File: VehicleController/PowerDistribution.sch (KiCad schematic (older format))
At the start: 15 parts, among them P3 RPi_USB_PWR, U2 TL431, U3 BTS6133D, U4 AP1117

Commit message: Nearly finished with VC Schematic
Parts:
- P3: symbol USB_A -> USB_A-RESCUE-VehicleController
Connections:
- net 5V renamed +5V
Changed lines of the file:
@@
 EESchema Schematic File Version 2
+LIBS:UNCAMotorsports
 LIBS:VehicleController-rescue
 LIBS:power
@@
 LIBS:contrib
 LIBS:valves
-LIBS:UNCAMotorsports
 LIBS:Common-Parts-Library-CPL
 LIBS:relays
@@
 $EndComp
 $Comp
-L GND #PWR26
+L GND #PWR026
 U 1 1 587C7BE3
 P 6000 3550
-F 0 "#PWR26" H 6000 3300 50  0001 C CNN
+F 0 "#PWR026" H 6000 3300 50  0001 C CNN
 F 1 "GND" H 6005 3377 50  0000 C CNN
 F 2 "" H 6000 3550 50  0000 C CNN
@@
 $EndComp
 $Comp
-L GND #PWR24
+L GND #PWR027
 U 1 1 587C7BF7
 P 4300 4700
-F 0 "#PWR24" H 4300 4450 50  0001 C CNN
+F 0 "#PWR027" H 4300 4450 50  0001 C CNN
 F 1 "GND" H 4305 4527 50  0000 C CNN
 F 2 "" H 4300 4700 50  0000 C CNN
@@
 $EndComp
 $Comp
-L GND #PWR28
+L GND #PWR028
 U 1 1 58AEB860
 P 8100 3250
-F 0 "#PWR28" H 8100 3000 50  0001 C CNN
+F 0 "#PWR028" H 8100 3000 50  0001 C CNN
 F 1 "GND" H 8105 3077 50  0000 C CNN
 F 2 "" H 8100 3250 50  0000 C CNN
@@
 Text HLabel 7350 2550 1    60   Input ~ 0
 12V
-Text HLabel 8900 2750 2    60   Input ~ 0
+Text HLabel 8850 2750 2    60   Input ~ 0
 5V
 $Comp
-L PWR_FLAG #FLG2
+L PWR_FLAG #FLG029
 U 1 1 58AF2028
 P 5550 1000
-F 0 "#FLG2" H 5550 1095 50  0001 C CNN
+F 0 "#FLG029" H 5550 1095 50  0001 C CNN
 F 1 "PWR_FLAG" H 5550 1224 50  0001 C CNN
 F 2 "" H 5550 1000 50  0000 C CNN
@@
 12V
 $Comp
-L PWR_FLAG #FLG3
-U 1 1 58AF2853
-P 5700 1000
-F 0 "#FLG3" H 5700 1095 50  0001 C CNN
-F 1 "PWR_FLAG" H 5700 1224 50  0001 C CNN
-F 2 "" H 5700 1000 50  0000 C CNN
-F 3 "" H 5700 1000 50  0000 C CNN
-	1    5700 1000
-	1    0    0    -1
-$EndComp
-$Comp
-L GND #PWR25
-U 1 1 58AF29E4
-P 5700 1200
-F 0 "#PWR25" H 5700 950 50  0001 C CNN
-F 1 "GND" H 5705 1027 50  0000 C CNN
-F 2 "" H 5700 1200 50  0000 C CNN
-F 3 "" H 5700 1200 50  0000 C CNN
-	1    5700 1200
-	1    0    0    -1
-$EndComp
-Text HLabel 5400 1200 3    60   Input ~ 0
-PWR_IN
-$Comp
-L PWR_FLAG #FLG1
-U 1 1 58AF2E1D
-P 5400 1000
-F 0 "#FLG1" H 5400 1095 50  0001 C CNN
-F 1 "PWR_FLAG" H 5400 1224 50  0000 C CNN
-F 2 "" H 5400 1000 50  0000 C CNN
-F 3 "" H 5400 1000 50  0000 C CNN
-	1    5400 1000
-	1    0    0    -1
-$EndComp
-$Comp
-L USB_A P3
+L USB_A-RESCUE-VehicleController P3
 U 1 1 58B30D8B
 P 8050 4350
+AR Path="/58B30D8B" Ref="P3"  Part="1"
+AR Path="/587C78BB/58B30D8B" Ref="P3"  Part="1"
 F 0 "P3" V 7625 4274 50  0000 C CNN
 F 1 "RPi_USB_PWR" V 7716 4274 50  0000 C CNN
@@
 $EndComp
 $Comp
-L GND #PWR27
+L GND #PWR030
 U 1 1 58B30D9F
 P 7950 4750
-F 0 "#PWR27" H 7950 4500 50  0001 C CNN
+F 0 "#PWR030" H 7950 4500 50  0001 C CNN
 F 1 "GND" H 7955 4577 50  0000 C CNN
 F 2 "" H 7950 4750 50  0000 C CNN
@@
 12V
 $Comp
-L GND #PWR29
+L GND #PWR031
 U 1 1 58B31164
 P 8700 4550
-F 0 "#PWR29" H 8700 4300 50  0001 C CNN
+F 0 "#PWR031" H 8700 4300 50  0001 C CNN
 F 1 "GND" H 8705 4377 50  0000 C CNN
 F 2 "" H 8700 4550 50  0000 C CNN
@@
 $EndComp
 $Comp
-L GND #PWR22
+L GND #PWR032
 U 1 1 58B0EFE3
 P 3350 3250
-F 0 "#PWR22" H 3350 3000 50  0001 C CNN
+F 0 "#PWR032" H 3350 3000 50  0001 C CNN
 F 1 "GND" H 3355 3077 50  0000 C CNN
 F 2 "" H 3350 3250 50  0000 C CNN
@@
 $EndComp
 $Comp
-L GND #PWR23
+L GND #PWR033
 U 1 1 58B0F09D
 P 3550 3250
-F 0 "#PWR23" H 3550 3000 50  0001 C CNN
+F 0 "#PWR033" H 3550 3000 50  0001 C CNN
 F 1 "GND" H 3555 3077 50  0000 C CNN
 F 2 "" H 3550 3250 50  0000 C CNN
@@
 	4300 4250 4300 4700
 Wire Wire Line
-	4300 4400 4850 4400
-Wire Wire Line
-	4850 4400 4850 4150
+	4850 4400 4300 4400
+Wire Wire Line
+	4850 4150 4850 4400
 Connection ~ 4300 4400
 Wire Wire Line
@@
 	8600 2900 8600 2750
 Wire Wire Line
-	8400 2750 8900 2750
+	8400 2750 8850 2750
 Connection ~ 7600 2750
 Connection ~ 8600 2750
@@
 Wire Wire Line
 	5550 1200 5550 1000
-Wire Wire Line
-	5700 1200 5700 1000
-Wire Wire Line
-	5400 1200 5400 1000
 Connection ~ 8550 4150
 Wire Wire Line
@@
 Wire Wire Line
 	4850 2850 4850 3550
+$Comp
+L +5V #PWR034
+U 1 1 58BE7A1A
+P 8750 2600
+F 0 "#PWR034" H 8800 2650 50  0001 C CNN
+F 1 "+5V" H 8765 2773 50  0000 C CNN
+F 2 "" H 0   -100 50  0001 C CNN
+F 3 "" H 0   -100 50  0001 C CNN
+	1    8750 2600
+	1    0    0    -1
+$EndComp
+Wire Wire Line
+	8750 2600 8750 2750
+Connection ~ 8750 2750
 $EndSCHEMATC

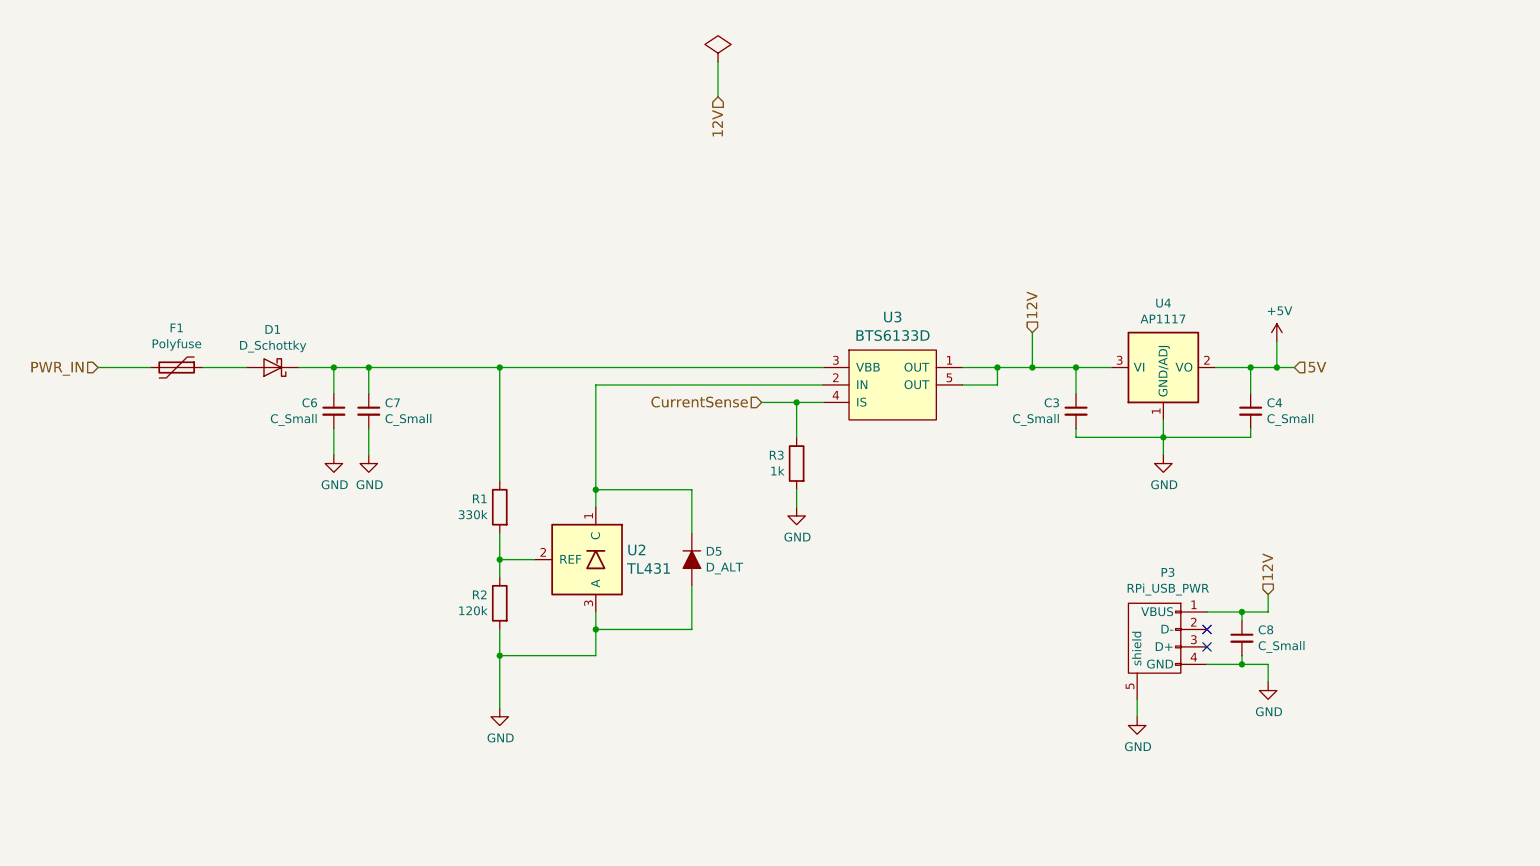
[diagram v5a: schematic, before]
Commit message: More status LEDs and fuses
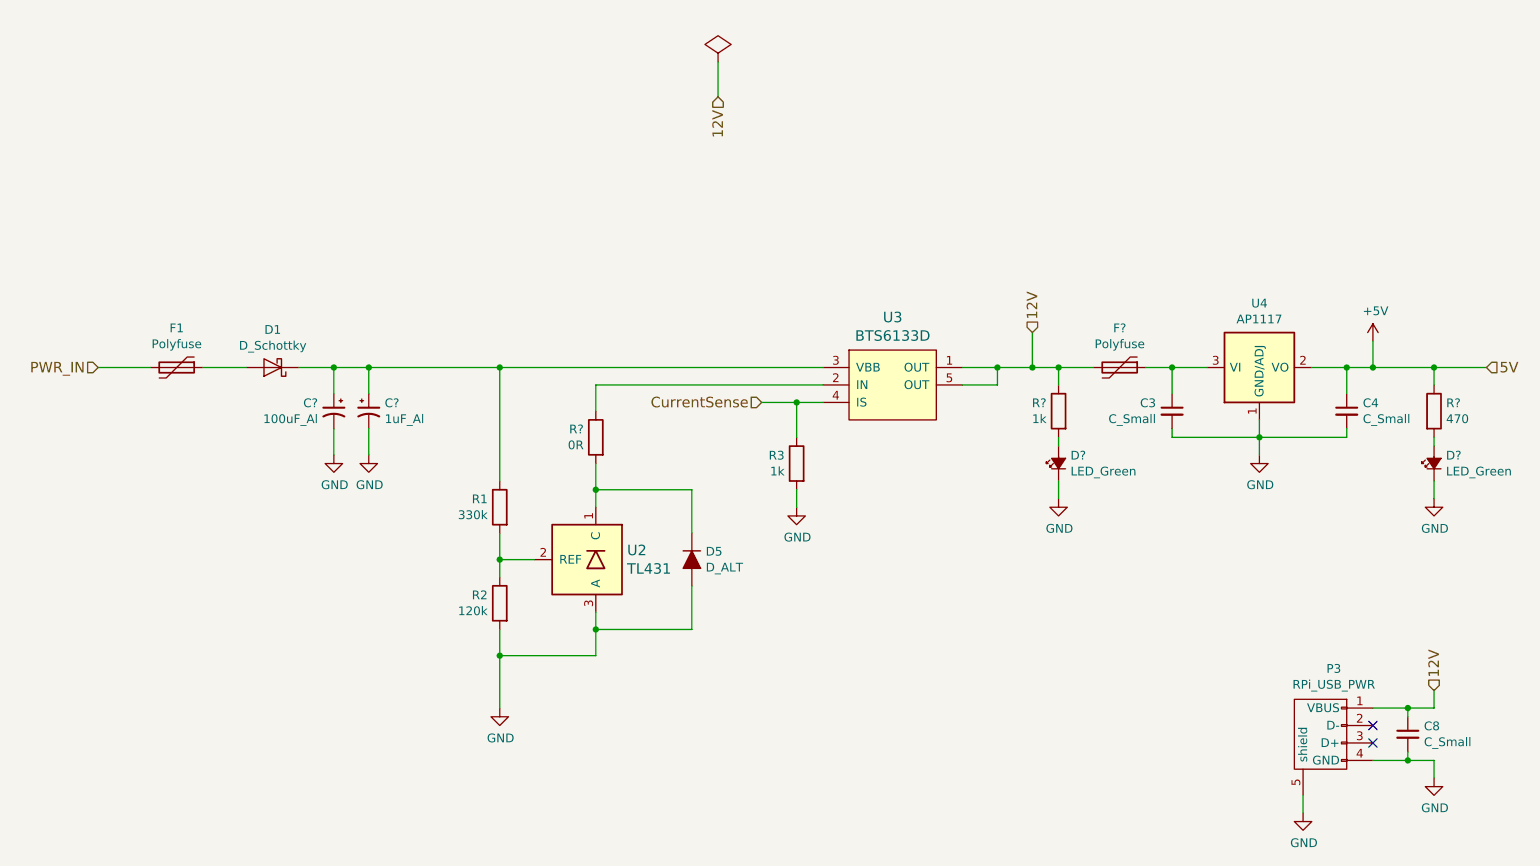
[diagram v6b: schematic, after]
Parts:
- removed C6, C7: C_Small, symbol C_Small
- added C?: 100uF_Al, symbol CP1_Small
- added C?: 1uF_Al, symbol CP1_Small
- added D? (x2): LED_Green, symbol LED_Small_ALT
- added F?: Polyfuse, symbol Polyfuse
- added R?: 1k, symbol R
- added R?: 470, symbol R
- added R?: 0R, symbol R
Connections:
- net +5V: now also R?.1
- net 12V: now also F?.2, R?.1; no longer C3.1, U4.3 (VI)
- net GND: now also C?.2, C?.2, D?.1 (K), D?.1 (K)
- net at D1.1 (K), R1.1, U3.3 (VBB): now also C?.1, C?.1
- net at D5.1 (K), U2.1 (C): now also R?.2; no longer U3.2 (IN)
- new net: R?.1, U3.2 (IN)
- new net: C3.1, F?.1, U4.3 (VI)
- new net: D?.2 (A), R?.2 (x2)
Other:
- moved on the sheet: C3, C4, C8, P3

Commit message: Begin nailing down VC schematic details
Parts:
- removed C8: C_Small, symbol C_Small
- removed U4: AP1117, TO_SOT_Packages_SMD:SOT-223, symbol AP1117
- added C9: 1uF_Al, symbol CP1_Small
- added U8: R-78E5.0-1.0, symbol R-78E5.0-1.0
- D6: renamed from D?; value LED_Green -> 12V_Status
- D7: renamed from D?; value LED_Green -> 5V_Status
- R14: renamed from R?; value 1k -> 2.2k
- gave numbers to parts that had none: 5
- renumbered C3 to C7, C4 to C8, D1 to D4, F1 to F2, P3 to P2, R1 to R10, R2 to R11, R3 to R13, U2 to U6, U3 to U7
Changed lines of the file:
@@
 $EndDescr
 $Comp
-L D_Schottky D1
+L D_Schottky D4
 U 1 1 587C7BB2
 P 3000 2750
-F 0 "D1" H 3000 2534 50  0000 C CNN
+F 0 "D4" H 3000 2534 50  0000 C CNN
 F 1 "D_Schottky" H 3000 2625 50  0000 C CNN
 F 2 "" H 3000 2750 50  0000 C CNN
@@
 $EndComp
 $Comp
-L Polyfuse F1
+L Polyfuse F2
 U 1 1 587C7BB9
 P 2450 2750
-F 0 "F1" V 2225 2750 50  0000 C CNN
+F 0 "F2" V 2225 2750 50  0000 C CNN
 F 1 "Polyfuse" V 2316 2750 50  0000 C CNN
 F 2 "" H 2500 2550 50  0001 L CNN
@@
 $EndComp
 $Comp
-L TL431 U2
+L TL431 U6
 U 1 1 587C7BC0
 P 4850 3850
-F 0 "U2" H 4671 3903 60  0000 R CNN
+F 0 "U6" H 4671 3903 60  0000 R CNN
 F 1 "TL431" H 4671 3797 60  0000 R CNN
 F 2 "" H 4850 3800 60  0000 C CNN
@@
 $EndComp
 $Comp
-L BTS6133D U3
+L BTS6133D U7
 U 1 1 587C7BC7
 P 6550 2850
-F 0 "U3" H 6550 3237 60  0000 C CNN
+F 0 "U7" H 6550 3237 60  0000 C CNN
 F 1 "BTS6133D" H 6550 3131 60  0000 C CNN
 F 2 "" H 6700 3050 60  0000 C CNN
@@
 $EndComp
 $Comp
-L R R1
+L R R10
 U 1 1 587C7BCE
 P 4300 3550
-F 0 "R1" H 4369 3596 50  0000 L CNN
+F 0 "R10" H 4369 3596 50  0000 L CNN
 F 1 "330k" H 4369 3505 50  0000 L CNN
 F 2 "" V 4230 3550 50  0000 C CNN
@@
 $EndComp
 $Comp
-L R R2
+L R R11
 U 1 1 587C7BD5
 P 4300 4100
-F 0 "R2" H 4369 4146 50  0000 L CNN
+F 0 "R11" H 4369 4146 50  0000 L CNN
 F 1 "120k" H 4369 4055 50  0000 L CNN
 F 2 "" V 4230 4100 50  0000 C CNN
@@
 $EndComp
 $Comp
-L R R3
+L R R13
 U 1 1 587C7BDC
 P 6000 3300
-F 0 "R3" H 6069 3346 50  0000 L CNN
+F 0 "R13" H 6069 3346 50  0000 L CNN
 F 1 "1k" H 6069 3255 50  0000 L CNN
 F 2 "" V 5930 3300 50  0000 C CNN
@@
 $EndComp
 $Comp
-L GND #PWR026
+L GND #PWR29
 U 1 1 587C7BE3
 P 6000 3550
-F 0 "#PWR026" H 6000 3300 50  0001 C CNN
+F 0 "#PWR29" H 6000 3300 50  0001 C CNN
 F 1 "GND" H 6005 3377 50  0000 C CNN
 F 2 "" H 6000 3550 50  0000 C CNN
@@
 $EndComp
 $Comp
-L GND #PWR027
+L GND #PWR28
 U 1 1 587C7BF7
 P 4300 4700
-F 0 "#PWR027" H 4300 4450 50  0001 C CNN
+F 0 "#PWR28" H 4300 4450 50  0001 C CNN
 F 1 "GND" H 4305 4527 50  0000 C CNN
 F 2 "" H 4300 4700 50  0000 C CNN
@@
 CurrentSense
 $Comp
-L C_Small C3
+L C_Small C7
 U 1 1 58AEB852
 P 8150 3000
-F 0 "C3" H 8242 3046 50  0000 L CNN
+F 0 "C7" H 8242 3046 50  0000 L CNN
 F 1 "C_Small" H 8242 2955 50  0000 L CNN
 F 2 "" H 8150 3000 50  0000 C CNN
@@
 $EndComp
 $Comp
-L C_Small C4
+L C_Small C8
 U 1 1 58AEB859
 P 9150 3000
-F 0 "C4" H 9242 3046 50  0000 L CNN
+F 0 "C8" H 9242 3046 50  0000 L CNN
 F 1 "C_Small" H 9242 2955 50  0000 L CNN
 F 2 "" H 9150 3000 50  0000 C CNN
@@
 $EndComp
 $Comp
-L GND #PWR028
+L GND #PWR31
 U 1 1 58AEB860
 P 8650 3250
-F 0 "#PWR028" H 8650 3000 50  0001 C CNN
+F 0 "#PWR31" H 8650 3000 50  0001 C CNN
 F 1 "GND" H 8655 3077 50  0000 C CNN
 F 2 "" H 8650 3250 50  0000 C CNN
@@
 5V
 $Comp
-L PWR_FLAG #FLG029
+L PWR_FLAG #FLG3
 U 1 1 58AF2028
 P 5550 1000
-F 0 "#FLG029" H 5550 1095 50  0001 C CNN
+F 0 "#FLG3" H 5550 1095 50  0001 C CNN
 F 1 "PWR_FLAG" H 5550 1224 50  0001 C CNN
 F 2 "" H 5550 1000 50  0000 C CNN
@@
 12V
 $Comp
-L USB_A-RESCUE-VehicleController P3
+L USB_A-RESCUE-VehicleController P2
 U 1 1 58B30D8B
 P 9000 4900
-AR Path="/58B30D8B" Ref="P3"  Part="1"
-AR Path="/587C78BB/58B30D8B" Ref="P3"  Part="1"
-F 0 "P3" V 8575 4824 50  0000 C CNN
+F 0 "P2" V 8575 4824 50  0000 C CNN
 F 1 "RPi_USB_PWR" V 8666 4824 50  0000 C CNN
 F 2 "" V 8950 4800 50  0000 C CNN
@@
 $EndComp
 $Comp
-L C_Small C8
-U 1 1 58B30D92
-P 9500 4850
-F 0 "C8" H 9592 4896 50  0000 L CNN
-F 1 "C_Small" H 9592 4805 50  0000 L CNN
-F 2 "" H 9500 4850 50  0000 C CNN
-F 3 "" H 9500 4850 50  0000 C CNN
-	1    9500 4850
-	1    0    0    -1
-$EndComp
-$Comp
-L GND #PWR030
+L GND #PWR32
 U 1 1 58B30D9F
 P 8900 5300
-F 0 "#PWR030" H 8900 5050 50  0001 C CNN
+F 0 "#PWR32" H 8900 5050 50  0001 C CNN
 F 1 "GND" H 8905 5127 50  0000 C CNN
 F 2 "" H 8900 5300 50  0000 C CNN
@@
 12V
 $Comp
-L GND #PWR031
+L GND #PWR35
 U 1 1 58B31164
 P 9650 5100
-F 0 "#PWR031" H 9650 4850 50  0001 C CNN
+F 0 "#PWR35" H 9650 4850 50  0001 C CNN
 F 1 "GND" H 9655 4927 50  0000 C CNN
 F 2 "" H 9650 5100 50  0000 C CNN
@@
 $EndComp
 $Comp
-L GND #PWR032
+L GND #PWR26
 U 1 1 58B0EFE3
 P 3350 3250
-F 0 "#PWR032" H 3350 3000 50  0001 C CNN
+F 0 "#PWR26" H 3350 3000 50  0001 C CNN
 F 1 "GND" H 3355 3077 50  0000 C CNN
 F 2 "" H 3350 3250 50  0000 C CNN
@@
 $EndComp
 $Comp
-L GND #PWR033
+L GND #PWR27
 U 1 1 58B0F09D
 P 3550 3250
-F 0 "#PWR033" H 3550 3000 50  0001 C CNN
+F 0 "#PWR27" H 3550 3000 50  0001 C CNN
 F 1 "GND" H 3555 3077 50  0000 C CNN
 F 2 "" H 3550 3250 50  0000 C CNN
@@
 	4850 3300 4850 3550
 $Comp
-L +5V #PWR034
+L +5V #PWR33
 U 1 1 58BE7A1A
 P 9300 2600
-F 0 "#PWR034" H 9350 2650 50  0001 C CNN
+F 0 "#PWR33" H 9350 2650 50  0001 C CNN
 F 1 "+5V" H 9315 2773 50  0000 C CNN
 F 2 "" H 550 -100 50  0001 C CNN
@@
 Connection ~ 9300 2750
 $Comp
-L AP1117 U4
-U 1 1 58C28B86
-P 8650 2750
-F 0 "U4" H 8650 3117 50  0000 C CNN
-F 1 "AP1117" H 8650 3026 50  0000 C CNN
-F 2 "TO_SOT_Packages_SMD:SOT-223" H 500 -350 50  0001 C CNN
-F 3 "" H 600 -250 50  0001 C CNN
-	1    8650 2750
-	1    0    0    -1
-$EndComp
-$Comp
-L Polyfuse F?
+L Polyfuse F3
 U 1 1 58C2ADFE
 P 7850 2750
-F 0 "F?" V 7625 2750 50  0000 C CNN
+F 0 "F3" V 7625 2750 50  0000 C CNN
 F 1 "Polyfuse" V 7716 2750 50  0000 C CNN
 F 2 "" H 7900 2550 50  0001 L CNN
@@
 $EndComp
 $Comp
-L R R?
+L R R14
 U 1 1 58C314B1
 P 7500 3000
-F 0 "R?" H 7569 3046 50  0000 L CNN
-F 1 "1k" H 7569 2955 50  0000 L CNN
+F 0 "R14" H 7569 3046 50  0000 L CNN
+F 1 "2.2k" H 7569 2955 50  0000 L CNN
 F 2 "" V 7430 3000 50  0000 C CNN
 F 3 "" H 7500 3000 50  0000 C CNN
@@
 $EndComp
 $Comp
-L LED_Small_ALT D?
+L LED_Small_ALT D6
 U 1 1 58C318C7
 P 7500 3300
-F 0 "D?" V 7546 3232 50  0000 R CNN
-F 1 "LED_Green" V 7455 3232 50  0000 R CNN
+F 0 "D6" V 7546 3232 50  0000 R CNN
+F 1 "12V_Status" V 7455 3232 50  0000 R CNN
 F 2 "" V 750 -300 50  0001 C CNN
 F 3 "" V 750 -300 50  0001 C CNN
@@
 Connection ~ 7500 2750
 $Comp
-L GND #PWR?
+L GND #PWR30
 U 1 1 58C31B60
 P 7500 3500
-F 0 "#PWR?" H 7500 3250 50  0001 C CNN
+F 0 "#PWR30" H 7500 3250 50  0001 C CNN
 F 1 "GND" H 7505 3327 50  0000 C CNN
 F 2 "" H 7500 3500 50  0000 C CNN
@@
 	7500 3500 7500 3400
 $Comp
-L LED_Small_ALT D?
+L LED_Small_ALT D7
 U 1 1 58C3218B
 P 9650 3300
-F 0 "D?" V 9696 3232 50  0000 R CNN
-F 1 "LED_Green" V 9605 3232 50  0000 R CNN
+F 0 "D7" V 9696 3232 50  0000 R CNN
+F 1 "5V_Status" V 9605 3232 50  0000 R CNN
 F 2 "" V 2900 -300 50  0001 C CNN
 F 3 "" V 2900 -300 50  0001 C CNN
@@
 $EndComp
 $Comp
-L R R?
+L R R15
 U 1 1 58C321FD
 P 9650 3000
-F 0 "R?" H 9719 3046 50  0000 L CNN
+F 0 "R15" H 9719 3046 50  0000 L CNN
 F 1 "470" H 9719 2955 50  0000 L CNN
 F 2 "" V 9580 3000 50  0000 C CNN
@@
 	9650 3200 9650 3150
 $Comp
-L GND #PWR?
+L GND #PWR34
 U 1 1 58C32364
 P 9650 3500
-F 0 "#PWR?" H 9650 3250 50  0001 C CNN
+F 0 "#PWR34" H 9650 3250 50  0001 C CNN
 F 1 "GND" H 9655 3327 50  0000 C CNN
 F 2 "" H 9650 3500 50  0000 C CNN
@@
 	9650 3500 9650 3400
 $Comp
-L CP1_Small C?
+L CP1_Small C5
 U 1 1 58C33250
 P 3350 3000
-F 0 "C?" H 3441 3046 50  0000 L CNN
+F 0 "C5" H 3441 3046 50  0000 L CNN
 F 1 "100uF_Al" H 3441 2955 50  0000 L CNN
 F 2 "" H 700 -350 50  0001 C CNN
@@
 $EndComp
 $Comp
-L CP1_Small C?
+L CP1_Small C6
 U 1 1 58C33352
 P 3550 3000
-F 0 "C?" H 3641 3046 50  0000 L CNN
+F 0 "C6" H 3641 3046 50  0000 L CNN
 F 1 "1uF_Al" H 3641 2955 50  0000 L CNN
 F 2 "" H 900 -350 50  0001 C CNN
@@
 $EndComp
 $Comp
-L R R?
+L R R12
 U 1 1 58C342F9
 P 4850 3150
-F 0 "R?" H 4919 3196 50  0000 L CNN
+F 0 "R12" H 4919 3196 50  0000 L CNN
 F 1 "0R" H 4919 3105 50  0000 L CNN
 F 2 "" V 4780 3150 50  0000 C CNN
@@
 Wire Wire Line
 	4850 3000 4850 2850
+$Comp
+L R-78E5.0-1.0 U8
+U 1 1 58C571BC
+P 8650 2750
+F 0 "U8" H 8650 3037 60  0000 C CNN
+F 1 "R-78E5.0-1.0" H 8650 2931 60  0000 C CNN
+F 2 "" H 2600 1150 60  0000 C CNN
+F 3 "" H 2600 1150 60  0000 C CNN
+	1    8650 2750
+	1    0    0    -1
+$EndComp
+$Comp
+L CP1_Small C9
+U 1 1 58C289B7
+P 9500 4850
+F 0 "C9" H 9591 4896 50  0000 L CNN
+F 1 "1uF_Al" H 9591 4805 50  0000 L CNN
+F 2 "" H 0   0   50  0001 C CNN
+F 3 "" H 0   0   50  0001 C CNN
+	1    9500 4850
+	1    0    0    -1
+$EndComp
 $EndSCHEMATC
